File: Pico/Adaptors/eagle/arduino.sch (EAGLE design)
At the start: 3 parts

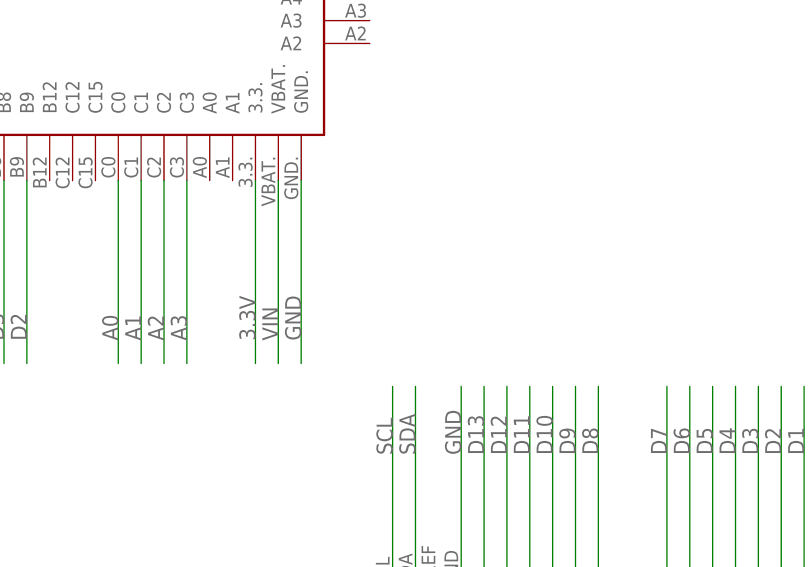
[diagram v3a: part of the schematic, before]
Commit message: Add I2C pullup
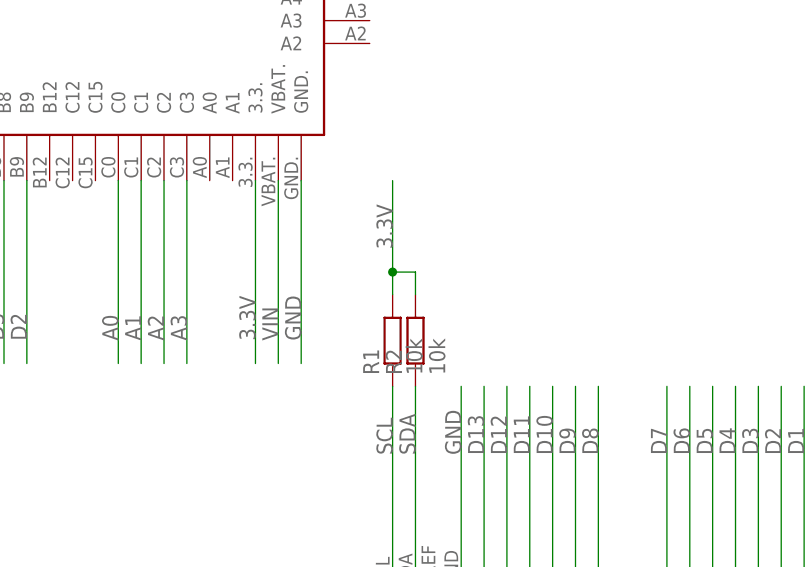
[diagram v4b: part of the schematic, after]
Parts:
- added R1, R2: 10k, rcl:R-EU_R0805
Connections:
- net 3.3V: now also R1.2, R2.2
- net SCL: now also R1.1
- net SDA: now also R2.1
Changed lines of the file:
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@@
 <part name="U$3" library="espruino_pico" deviceset="ESPRUINO" device=""/>
 <part name="U$1" library="espruino_pico" deviceset="ESPRUINO_PICO_SMDONLY" device=""/>
+<part name="R1" library="rcl" deviceset="R-EU_" device="R0805" value="10k"/>
+<part name="R2" library="rcl" deviceset="R-EU_" device="R0805" value="10k"/>
 </parts>
 <sheets>
@@
 <instance part="U$3" gate="G$1" x="22.86" y="132.08" rot="R90"/>
 <instance part="U$1" gate="G$1" x="-7.62" y="43.18"/>
+<instance part="R1" gate="G$1" x="60.96" y="78.74" rot="R90"/>
+<instance part="R2" gate="G$1" x="63.5" y="78.74" rot="R90"/>
 </instances>
 <busses>
@@
 <label x="-10.16" y="7.62" size="1.778" layer="95" rot="R90"/>
 </segment>
+<segment>
+<pinref part="R1" gate="G$1" pin="2"/>
+<wire x1="60.96" y1="83.82" x2="60.96" y2="86.36" width="0.1524" layer="91"/>
+<wire x1="60.96" y1="86.36" x2="60.96" y2="96.52" width="0.1524" layer="91"/>
+<wire x1="60.96" y1="86.36" x2="63.5" y2="86.36" width="0.1524" layer="91"/>
+<pinref part="R2" gate="G$1" pin="2"/>
+<wire x1="63.5" y1="86.36" x2="63.5" y2="83.82" width="0.1524" layer="91"/>
+<junction x="60.96" y="86.36"/>
+<label x="60.96" y="88.9" size="1.778" layer="95" rot="R90"/>
+</segment>
 </net>
 <net name="SCL" class="0">
@@
 <wire x1="60.96" y1="53.34" x2="60.96" y2="73.66" width="0.1524" layer="91"/>
 <label x="60.96" y="66.04" size="1.778" layer="95" rot="R90"/>
+<pinref part="R1" gate="G$1" pin="1"/>
 </segment>
 <segment>
@@
 <wire x1="63.5" y1="53.34" x2="63.5" y2="73.66" width="0.1524" layer="91"/>
 <label x="63.5" y="66.04" size="1.778" layer="95" rot="R90"/>
-</segment>
-<segment>
+<pinref part="R2" gate="G$1" pin="1"/>
+</segment>
+<segment>

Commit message: a full panel
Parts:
- added J1: JST-2P-SMD-PW-3410050P1, OPL Eagle Library:JST-2P-SMD-PW-3410050P1
- U$1: value ESPRUINO_PICO_SMDONLY -> ESPRUINO_PICO_SMD; device espruino_pico:ESPRUINO_PICO_SMDONLY -> espruino_pico:ESPRUINO_PICO_SMD
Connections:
- new net N$1: J1.+, U$1.BAT
- net GND: now also J1.-, J1.3, J1.4
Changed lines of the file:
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@@
 <?xml version="1.0" encoding="utf-8"?>
 <!DOCTYPE eagle SYSTEM "eagle.dtd">
-<eagle version="6.5.0">
+<eagle version="7.4.0">
 <drawing>
 <settings>
@@
 <layers>
 <layer number="1" name="Top" color="4" fill="1" visible="no" active="no"/>
+<layer number="2" name="Route2" color="1" fill="3" visible="no" active="no"/>
+<layer number="15" name="Route15" color="4" fill="6" visible="no" active="no"/>
 <layer number="16" name="Bottom" color="1" fill="1" visible="no" active="no"/>
 <layer number="17" name="Pads" color="2" fill="1" visible="no" active="no"/>
@@
 <layer number="106" name="bPlate" color="7" fill="1" visible="yes" active="yes"/>
 <layer number="107" name="Crop" color="7" fill="1" visible="yes" active="yes"/>
+<layer number="108" name="fp8" color="7" fill="1" visible="no" active="no"/>
+<layer number="109" name="fp9" color="7" fill="1" visible="no" active="no"/>
+<layer number="110" name="110" color="7" fill="1" visible="no" active="no"/>
+<layer number="111" name="111" color="7" fill="1" visible="no" active="no"/>
+<layer number="112" name="tSilk" color="7" fill="1" visible="no" active="no"/>
 <layer number="116" name="Patch_BOT" color="9" fill="4" visible="yes" active="yes"/>
+<layer number="118" name="Rect_Pads" color="7" fill="1" visible="no" active="no"/>
 <layer number="121" name="_tsilk" color="7" fill="1" visible="yes" active="yes"/>
 <layer number="122" name="_bsilk" color="7" fill="1" visible="yes" active="yes"/>
+<layer number="123" name="tTestmark" color="7" fill="1" visible="no" active="no"/>
+<layer number="124" name="bTestmark" color="7" fill="1" visible="no" active="no"/>
 <layer number="125" name="_tNames" color="7" fill="1" visible="yes" active="yes"/>
+<layer number="126" name="_bNames" color="7" fill="1" visible="no" active="no"/>
+<layer number="127" name="_tValues" color="7" fill="1" visible="no" active="no"/>
+<layer number="128" name="_bValues" color="7" fill="1" visible="no" active="no"/>
+<layer number="131" name="tAdjust" color="7" fill="1" visible="no" active="no"/>
+<layer number="132" name="bAdjust" color="7" fill="1" visible="no" active="no"/>
 <layer number="144" name="Drill_legend" color="7" fill="1" visible="yes" active="yes"/>
 <layer number="151" name="HeatSink" color="7" fill="1" visible="yes" active="yes"/>
+<layer number="152" name="_bDocu" color="7" fill="1" visible="no" active="no"/>
+<layer number="199" name="Contour" color="7" fill="1" visible="no" active="no"/>
 <layer number="200" name="200bmp" color="1" fill="10" visible="yes" active="yes"/>
 <layer number="201" name="201bmp" color="2" fill="10" visible="yes" active="yes"/>
@@
 <layer number="223" name="223bmp" color="24" fill="1" visible="no" active="no"/>
 <layer number="224" name="224bmp" color="25" fill="1" visible="no" active="no"/>
+<layer number="248" name="Housing" color="7" fill="1" visible="no" active="no"/>
+<layer number="249" name="Edge" color="7" fill="1" visible="no" active="no"/>
 <layer number="250" name="Descript" color="3" fill="1" visible="no" active="no"/>
 <layer number="251" name="SMDround" color="12" fill="11" visible="no" active="no"/>
@@
 <part name="U$2" library="arduino" deviceset="ARDUINO" device=""/>
 <part name="U$3" library="espruino_pico" deviceset="ESPRUINO" device=""/>
-<part name="U$1" library="espruino_pico" deviceset="ESPRUINO_PICO_SMDONLY" device=""/>
+<part name="U$1" library="espruino_pico" deviceset="ESPRUINO_PICO_SMD" device=""/>
 <part name="R1" library="rcl" deviceset="R-EU_" device="R0805" value="10k"/>
 <part name="R2" library="rcl" deviceset="R-EU_" device="R0805" value="10k"/>
+<part name="J1" library="OPL Eagle Library" deviceset="JST-2P-SMD-PW" device="-3410050P1"/>
 </parts>
 <sheets>
@@
 <instance part="R1" gate="G$1" x="60.96" y="78.74" rot="R90"/>
 <instance part="R2" gate="G$1" x="63.5" y="78.74" rot="R90"/>
+<instance part="J1" gate="J" x="-17.78" y="78.74" rot="R270"/>
 </instances>
 <busses>
@@
 <label x="-15.24" y="7.62" size="1.778" layer="95" rot="R90"/>
 </segment>
+<segment>
+<pinref part="J1" gate="J" pin="-"/>
+<wire x1="-20.32" y1="73.025" x2="-20.32" y2="71.12" width="0.1524" layer="91"/>
+<wire x1="-20.32" y1="71.12" x2="-20.32" y2="58.42" width="0.1524" layer="91"/>
+<wire x1="-20.32" y1="71.12" x2="-27.94" y2="71.12" width="0.1524" layer="91"/>
+<wire x1="-27.94" y1="71.12" x2="-27.94" y2="78.74" width="0.1524" layer="91"/>
+<wire x1="-27.94" y1="78.74" x2="-27.94" y2="83.82" width="0.1524" layer="91"/>
+<wire x1="-27.94" y1="83.82" x2="-7.62" y2="83.82" width="0.1524" layer="91"/>
+<wire x1="-7.62" y1="83.82" x2="-7.62" y2="78.74" width="0.1524" layer="91"/>
+<wire x1="-7.62" y1="78.74" x2="-11.43" y2="78.74" width="0.1524" layer="91"/>
+<wire x1="-27.94" y1="78.74" x2="-24.13" y2="78.74" width="0.1524" layer="91"/>
+<pinref part="J1" gate="J" pin="3"/>
+<pinref part="J1" gate="J" pin="4"/>
+<label x="-20.32" y="60.96" size="1.778" layer="95" rot="R90"/>
+</segment>
 </net>
 <net name="VIN" class="1">
@@
 </segment>
 </net>
+<net name="N$1" class="0">
+<segment>
+<pinref part="U$1" gate="G$1" pin="BAT"/>
+<pinref part="J1" gate="J" pin="+"/>
+<wire x1="-15.24" y1="73.025" x2="-15.24" y2="50.8" width="0.1524" layer="91"/>
+</segment>
+</net>
